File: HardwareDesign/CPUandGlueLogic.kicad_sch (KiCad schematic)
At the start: 33 parts, among them J100 Conn_01x02, U101 74HCT245, U102 74HCT245, U103 74HCT245, U104 74HCT365, U105 MAX708, U106 HD6809, U107 74HCT00, U108 74HCT27, U109 74HCT138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

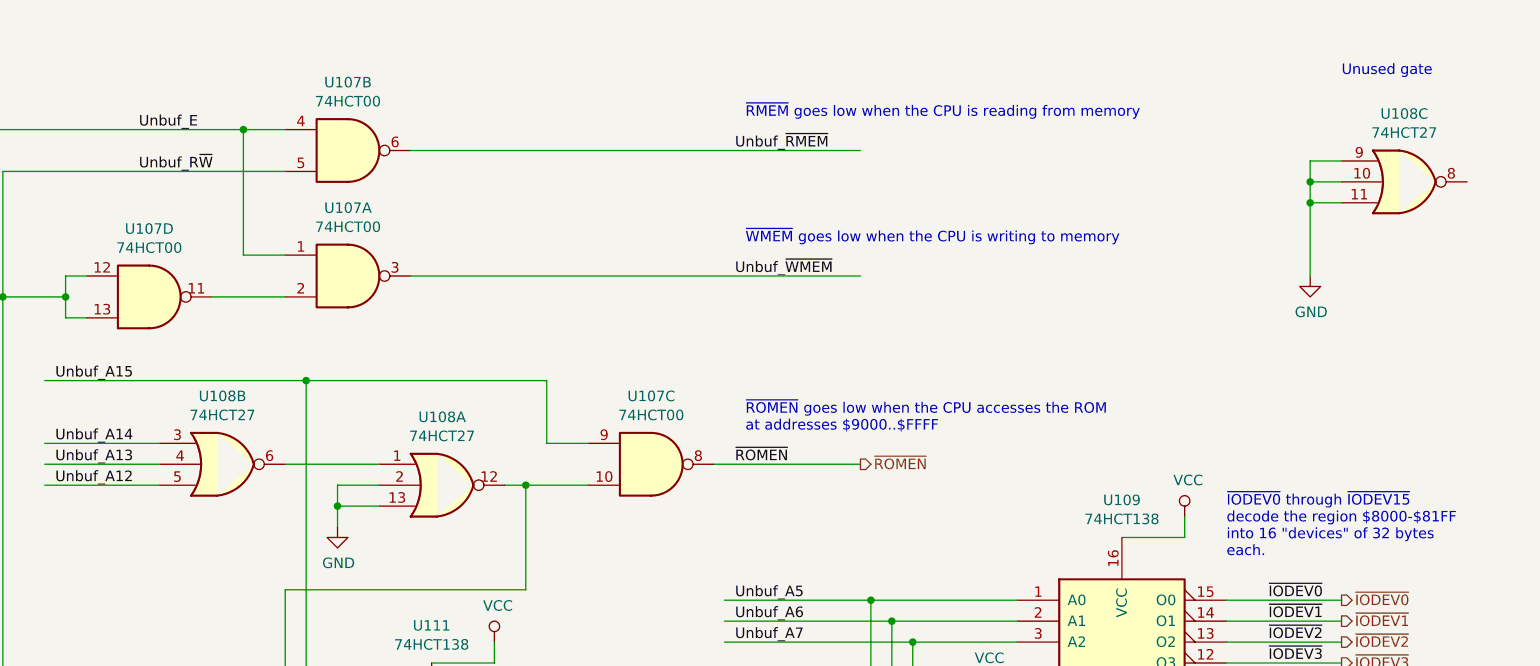
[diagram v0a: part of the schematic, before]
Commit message: initial schematic for FPGA display controller
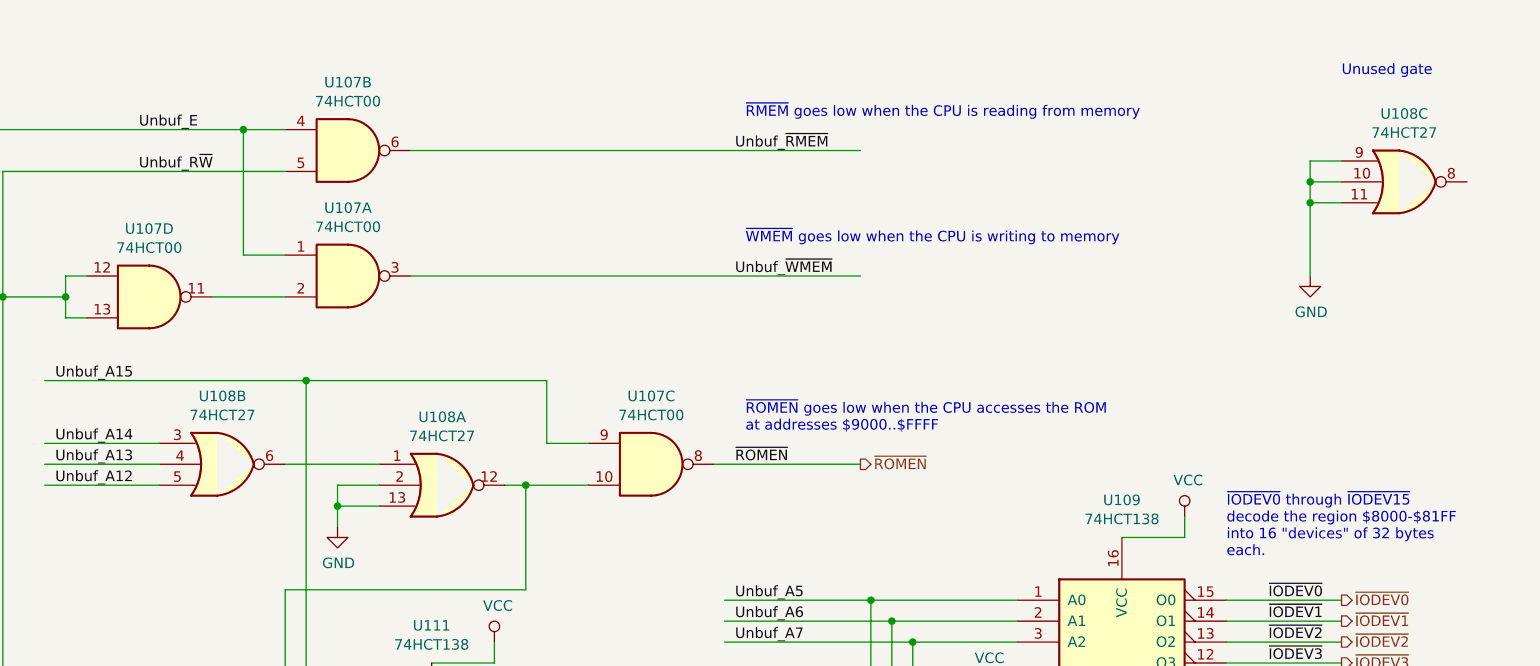
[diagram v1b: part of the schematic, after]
